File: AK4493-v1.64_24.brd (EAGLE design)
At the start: 89.9 x 64 mm, 138 parts, among them IC2 AK4493, IC3 AK4493, IC4A SN74ABT273DBR

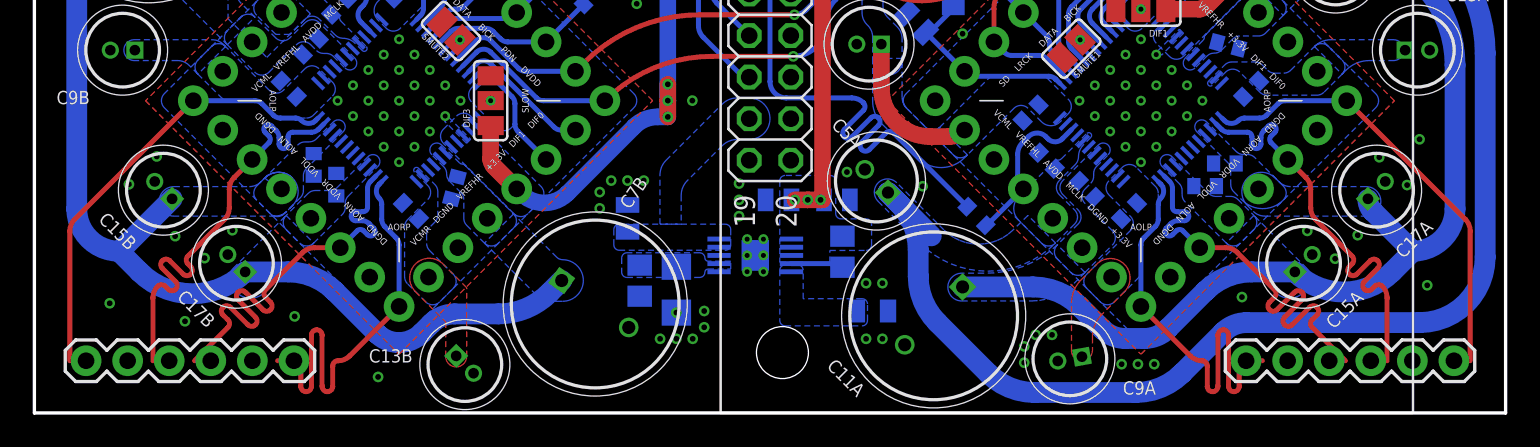
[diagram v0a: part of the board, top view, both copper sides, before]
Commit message: Fixed length of traces
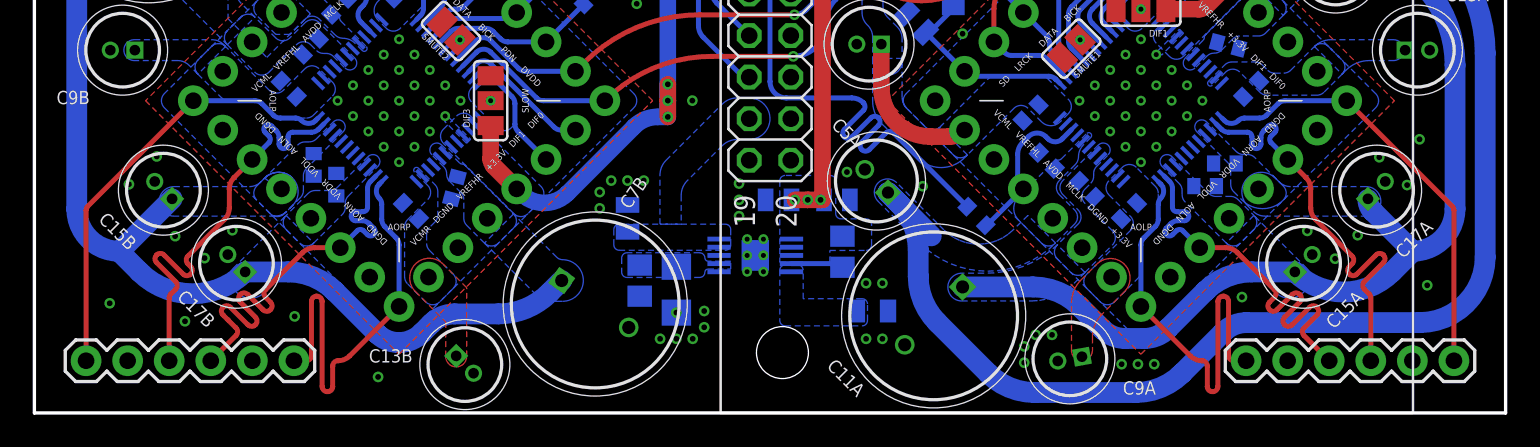
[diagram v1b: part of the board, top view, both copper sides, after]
